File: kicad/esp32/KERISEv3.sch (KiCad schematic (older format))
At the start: 22 parts, among them P1 ANT, SW1 RESET, U1 ESP32, U2 XTAL, U3 FLASH

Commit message: 自動配線成功
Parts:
- removed C1, C6, C7: 0.1u, Capacitors_SMD:C_0201, symbol C_Small
- removed C12: 3.9p, Capacitors_SMD:C_0201, symbol C_Small
- removed C14: 2.4p, Capacitors_SMD:C_0201, symbol C_Small
- removed L1: 2.7n, Capacitors_SMD:C_0201, symbol L_Small
- removed P1: ANT, mouse:SMD_conn_2, symbol CONN_01X02
- C5: renamed from C8; value 3300p -> 3.3n
- U2: footprint Crystals:crystal_FA238-TSX3225 -> mouse:crystal_FA238-TSX3225
- U3: footprint Power_Integrations:SO-8 -> mouse:SOIJ-8_5.3x5.3mm_Pitch1.27mm
- renumbered C2 to C1, C3 to C2, C4 to C3, C5 to C4, C9 to C6, C10 to C7, C11 to C8, C13 to C9
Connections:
- wire segments 115 -> 106
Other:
- moved on the sheet: C4
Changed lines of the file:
@@
 $Descr A4 11693 8268
 encoding utf-8
-Sheet 1 13
+Sheet 1 14
 Title ""
 Date ""
@@
 Main
 $Comp
-L C_Small C1
-U 1 1 5894E609
-P 9500 1300
-F 0 "C1" H 9510 1370 50  0000 L CNN
-F 1 "0.1u" H 9510 1220 50  0000 L CNN
-F 2 "Capacitors_SMD:C_0201" H 9500 1300 50  0001 C CNN
-F 3 "" H 9500 1300 50  0000 C CNN
-	1    9500 1300
-	0    1    1    0
-$EndComp
-$Comp
-L C_Small C5
+L C_Small C4
 U 1 1 5894E774
-P 9500 2100
-F 0 "C5" H 9510 2170 50  0000 L CNN
-F 1 "0.1u" H 9510 2020 50  0000 L CNN
-F 2 "Capacitors_SMD:C_0201" H 9500 2100 50  0001 C CNN
-F 3 "" H 9500 2100 50  0000 C CNN
-	1    9500 2100
-	0    1    1    0
-$EndComp
-$Comp
-L C_Small C7
-U 1 1 5894E88A
-P 9500 2500
-F 0 "C7" H 9510 2570 50  0000 L CNN
-F 1 "0.1u" H 9510 2420 50  0000 L CNN
-F 2 "Capacitors_SMD:C_0201" H 9500 2500 50  0001 C CNN
-F 3 "" H 9500 2500 50  0000 C CNN
-	1    9500 2500
+P 9500 2300
+F 0 "C4" H 9510 2370 50  0000 L CNN
+F 1 "0.1u" H 9510 2220 50  0000 L CNN
+F 2 "Capacitors_SMD:C_0201" H 9500 2300 50  0001 C CNN
+F 3 "" H 9500 2300 50  0000 C CNN
+	1    9500 2300
 	0    1    1    0
 $EndComp
@@
 Text GLabel 5000 3600 0    50   Input ~ 0
 SPEAKER
-Text GLabel 5000 4400 0    50   Input ~ 0
+Text GLabel 5000 4000 0    50   Input ~ 0
 AXIS_~CS
-Text GLabel 5000 4000 0    50   Input ~ 0
+Text GLabel 5000 4100 0    50   Input ~ 0
 AXIS_SCK
 Text GLabel 5000 4200 0    50   Input ~ 0
 AXIS_MOSI
-Text GLabel 5000 4100 0    50   Input ~ 0
+Text GLabel 5000 4500 0    50   Input ~ 0
 AXIS_MISO
-Text GLabel 5000 4500 0    50   Input ~ 0
+Text GLabel 5000 4400 0    50   Input ~ 0
 BAT-VOL
 Text GLabel 5200 1500 0    50   Input ~ 0
@@
 $EndComp
 $Comp
-L C_Small C8
+L C_Small C5
 U 1 1 58A71512
 P 9700 4200
-F 0 "C8" H 9710 4270 50  0000 L CNN
-F 1 "3300p" H 9710 4120 50  0000 L CNN
+F 0 "C5" H 9710 4270 50  0000 L CNN
+F 1 "3.3n" H 9710 4120 50  0000 L CNN
 F 2 "Capacitors_SMD:C_0201" H 9700 4200 50  0001 C CNN
 F 3 "" H 9700 4200 50  0000 C CNN
@@
 $EndComp
 $Comp
-L C_Small C9
+L C_Small C6
 U 1 1 58A770D7
 P 10000 4200
-F 0 "C9" H 10010 4270 50  0000 L CNN
+F 0 "C6" H 10010 4270 50  0000 L CNN
 F 1 "0.01u" H 10010 4120 50  0000 L CNN
 F 2 "Capacitors_SMD:C_0201" H 10000 4200 50  0001 C CNN
@@
 $EndComp
 $Comp
-L C_Small C6
-U 1 1 58A93D5D
-P 9500 2300
-F 0 "C6" H 9510 2370 50  0000 L CNN
-F 1 "0.1u" H 9510 2220 50  0000 L CNN
-F 2 "Capacitors_SMD:C_0201" H 9500 2300 50  0001 C CNN
-F 3 "" H 9500 2300 50  0000 C CNN
-	1    9500 2300
-	0    1    1    0
-$EndComp
-$Comp
-L C_Small C3
+L C_Small C2
 U 1 1 58A9401A
 P 9500 1700
-F 0 "C3" H 9510 1770 50  0000 L CNN
+F 0 "C2" H 9510 1770 50  0000 L CNN
 F 1 "10u" H 9510 1620 50  0000 L CNN
 F 2 "Capacitors_SMD:C_0402" H 9500 1700 50  0001 C CNN
@@
 $EndComp
 $Comp
-L C_Small C2
+L C_Small C1
 U 1 1 58A94440
 P 9500 1500
-F 0 "C2" H 9510 1570 50  0000 L CNN
+F 0 "C1" H 9510 1570 50  0000 L CNN
 F 1 "0.1u" H 9510 1420 50  0000 L CNN
 F 2 "Capacitors_SMD:C_0201" H 9500 1500 50  0001 C CNN
@@
 F 0 "U3" H 5850 6450 60  0000 C CNN
 F 1 "FLASH" H 5900 6350 60  0000 C CNN
-F 2 "Power_Integrations:SO-8" H 5700 6250 60  0001 C CNN
+F 2 "mouse:SOIJ-8_5.3x5.3mm_Pitch1.27mm" H 5700 6250 60  0001 C CNN
 F 3 "" H 5700 6250 60  0000 C CNN
 	1    5700 6250
@@
 SDI/SD1
 $Comp
-L C_Small C13
+L C_Small C9
 U 1 1 58ABA852
 P 5100 5900
-F 0 "C13" H 5110 5970 50  0000 L CNN
+F 0 "C9" H 5110 5970 50  0000 L CNN
 F 1 "1u" H 5110 5820 50  0000 L CNN
 F 2 "Capacitors_SMD:C_0402" H 5100 5900 50  0001 C CNN
@@
 F 0 "U2" H 10300 5150 60  0000 C CNN
 F 1 "XTAL" H 10300 5000 60  0000 C CNN
-F 2 "Crystals:crystal_FA238-TSX3225" H 10300 4850 60  0001 C CNN
+F 2 "mouse:crystal_FA238-TSX3225" H 10300 4850 60  0001 C CNN
 F 3 "" H 10300 4850 60  0000 C CNN
 	1    10300 4850
@@
 	2600 5100 2500 5100
 Wire Wire Line
-	9200 1300 9400 1300
-Wire Wire Line
 	9200 1500 9400 1500
 Wire Wire Line
@@
 	9200 1900 9400 1900
 Connection ~ 9300 1700
-Wire Wire Line
-	9200 2100 9400 2100
 Connection ~ 9300 1900
-Wire Wire Line
-	9200 2300 9400 2300
 Connection ~ 9300 2100
 Wire Wire Line
-	9200 2500 9400 2500
-Connection ~ 9300 2300
-Connection ~ 9300 2500
-Wire Wire Line
-	9700 2100 9600 2100
-Wire Wire Line
 	9700 1900 9600 1900
-Connection ~ 9700 2100
-Wire Wire Line
-	9600 1300 9700 1300
 Connection ~ 9700 1900
 Connection ~ 9300 1300
@@
 	9700 3300 9600 3300
 Wire Wire Line
-	9700 2500 9600 2500
-Connection ~ 9700 2500
-Wire Wire Line
-	9700 2300 9600 2300
-Connection ~ 9700 2300
-Wire Wire Line
 	9600 1500 9700 1500
-Connection ~ 9700 1500
 Wire Wire Line
 	9700 1700 9600 1700
 Connection ~ 9700 1700
 Wire Wire Line
-	9700 1300 9700 2600
-Wire Wire Line
 	5100 6000 5100 6100
 Wire Wire Line
@@
 	9200 4000 10000 4000
 $Comp
-L C_Small C11
+L C_Small C8
 U 1 1 58ADFB26
 P 9700 5100
-F 0 "C11" H 9710 5170 50  0000 L CNN
+F 0 "C8" H 9710 5170 50  0000 L CNN
 F 1 "22p" H 9710 5020 50  0000 L CNN
 F 2 "Capacitors_SMD:C_0201" H 9700 5100 50  0001 C CNN
@@
 $EndComp
 $Comp
-L C_Small C10
+L C_Small C7
 U 1 1 58ADFC50
 P 9500 5100
-F 0 "C10" H 9510 5170 50  0000 L CNN
+F 0 "C7" H 9510 5170 50  0000 L CNN
 F 1 "22p" H 9510 5020 50  0000 L CNN
 F 2 "Capacitors_SMD:C_0201" H 9500 5100 50  0001 C CNN
@@
 $EndComp
 $Comp
-L C_Small C4
+L C_Small C3
 U 1 1 58AFD8EC
 P 9500 1900
-F 0 "C4" H 9510 1970 50  0000 L CNN
+F 0 "C3" H 9510 1970 50  0000 L CNN
 F 1 "10u" H 9510 1820 50  0000 L CNN
 F 2 "Capacitors_SMD:C_0402" H 9500 1900 50  0001 C CNN
@@
 	0    1    1    0
 $EndComp
-$Comp
-L L_Small L1
-U 1 1 58B5F4E4
-P 8000 5900
-F 0 "L1" H 8030 5940 50  0000 L CNN
-F 1 "2.7n" H 8030 5860 50  0000 L CNN
-F 2 "Capacitors_SMD:C_0201" H 8000 5900 50  0001 C CNN
-F 3 "" H 8000 5900 50  0000 C CNN
-	1    8000 5900
-	1    0    0    -1
-$EndComp
-$Comp
-L C_Small C12
-U 1 1 58B5F6D3
-P 7800 5700
-F 0 "C12" H 7810 5770 50  0000 L CNN
-F 1 "3.9p" H 7810 5620 50  0000 L CNN
-F 2 "Capacitors_SMD:C_0201" H 7800 5700 50  0001 C CNN
-F 3 "" H 7800 5700 50  0000 C CNN
-	1    7800 5700
-	0    1    1    0
-$EndComp
-$Comp
-L C_Small C14
-U 1 1 58B60E12
-P 7500 5900
-F 0 "C14" H 7510 5970 50  0000 L CNN
-F 1 "2.4p" H 7510 5820 50  0000 L CNN
-F 2 "Capacitors_SMD:C_0201" H 7500 5900 50  0001 C CNN
-F 3 "" H 7500 5900 50  0000 C CNN
-	1    7500 5900
-	1    0    0    -1
-$EndComp
-$Comp
-L GND #PWR013
-U 1 1 58B61357
-P 7500 6100
-F 0 "#PWR013" H 7500 5850 50  0001 C CNN
-F 1 "GND" H 7500 5950 50  0000 C CNN
-F 2 "" H 7500 6100 50  0000 C CNN
-F 3 "" H 7500 6100 50  0000 C CNN
-	1    7500 6100
-	1    0    0    -1
-$EndComp
-Wire Wire Line
-	7500 6100 7500 6000
-$Comp
-L GND #PWR014
-U 1 1 58B61565
-P 8000 6100
-F 0 "#PWR014" H 8000 5850 50  0001 C CNN
-F 1 "GND" H 8000 5950 50  0000 C CNN
-F 2 "" H 8000 6100 50  0000 C CNN
-F 3 "" H 8000 6100 50  0000 C CNN
-	1    8000 6100
-	1    0    0    -1
-$EndComp
-Wire Wire Line
-	8000 6100 8000 6000
-Wire Wire Line
-	8000 5800 8000 5700
-Wire Wire Line
-	7300 5700 7700 5700
-Wire Wire Line
-	7500 5700 7500 5800
-$Comp
-L CONN_01X02 P1
-U 1 1 58B61A43
-P 7100 5750
-F 0 "P1" H 7100 5900 50  0000 C CNN
-F 1 "ANT" V 7200 5750 50  0000 C CNN
-F 2 "mouse:SMD_conn_2" H 7100 5750 50  0001 C CNN
-F 3 "" H 7100 5750 50  0000 C CNN
-	1    7100 5750
-	-1   0    0    -1
-$EndComp
-$Comp
-L GND #PWR015
-U 1 1 58B61E88
-P 7300 6100
-F 0 "#PWR015" H 7300 5850 50  0001 C CNN
-F 1 "GND" H 7300 5950 50  0000 C CNN
-F 2 "" H 7300 6100 50  0000 C CNN
-F 3 "" H 7300 6100 50  0000 C CNN
-	1    7300 6100
-	1    0    0    -1
-$EndComp
-Wire Wire Line
-	7300 6100 7300 5800
-Connection ~ 7500 5700
-Connection ~ 8000 5700
-Text GLabel 8100 5700 2    50   Input ~ 0
+Text GLabel 2600 7300 2    50   Input ~ 0
 ANT
-Wire Wire Line
-	8100 5700 7900 5700
 Text GLabel 5200 1300 0    50   Input ~ 0
 ANT
@@
 Wire Wire Line
 	5000 2900 5200 2900
+Wire Wire Line
+	9300 2500 9200 2500
+Wire Wire Line
+	9200 2300 9400 2300
+Connection ~ 9300 2300
+Wire Wire Line
+	9300 1300 9200 1300
+Wire Wire Line
+	9700 1500 9700 2600
+Wire Wire Line
+	9300 2100 9200 2100
+Wire Wire Line
+	9600 2300 9700 2300
+Connection ~ 9700 2300
+$Sheet
+S 1500 7200 1000 200
+U 58A6C6D7
+F0 "Antena" 60
+F1 "Antena.sch" 60
+F2 "Antena_IN" I R 2500 7300 60
+$EndSheet
+Wire Wire Line
+	2600 7300 2500 7300
 $EndSCHEMATC

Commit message: 更新
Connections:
- net labels removed: LED_3, RESET
- wire segments 106 -> 104
- no-connect marks 2 -> 3

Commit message: ESP32の回路図を更新
BOOTに必要なピンを明記
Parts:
- U1: symbol ESP32 -> ESP32-RESCUE-KERISEv3
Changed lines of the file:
@@
 EESchema Schematic File Version 2
+LIBS:KERISEv3-rescue
 LIBS:power
 LIBS:device
@@
 NoConn ~ 5200 5100
 $Comp
-L ESP32 U1
+L ESP32-RESCUE-KERISEv3 U1
 U 1 1 58A3B0F8
 P 7200 3100

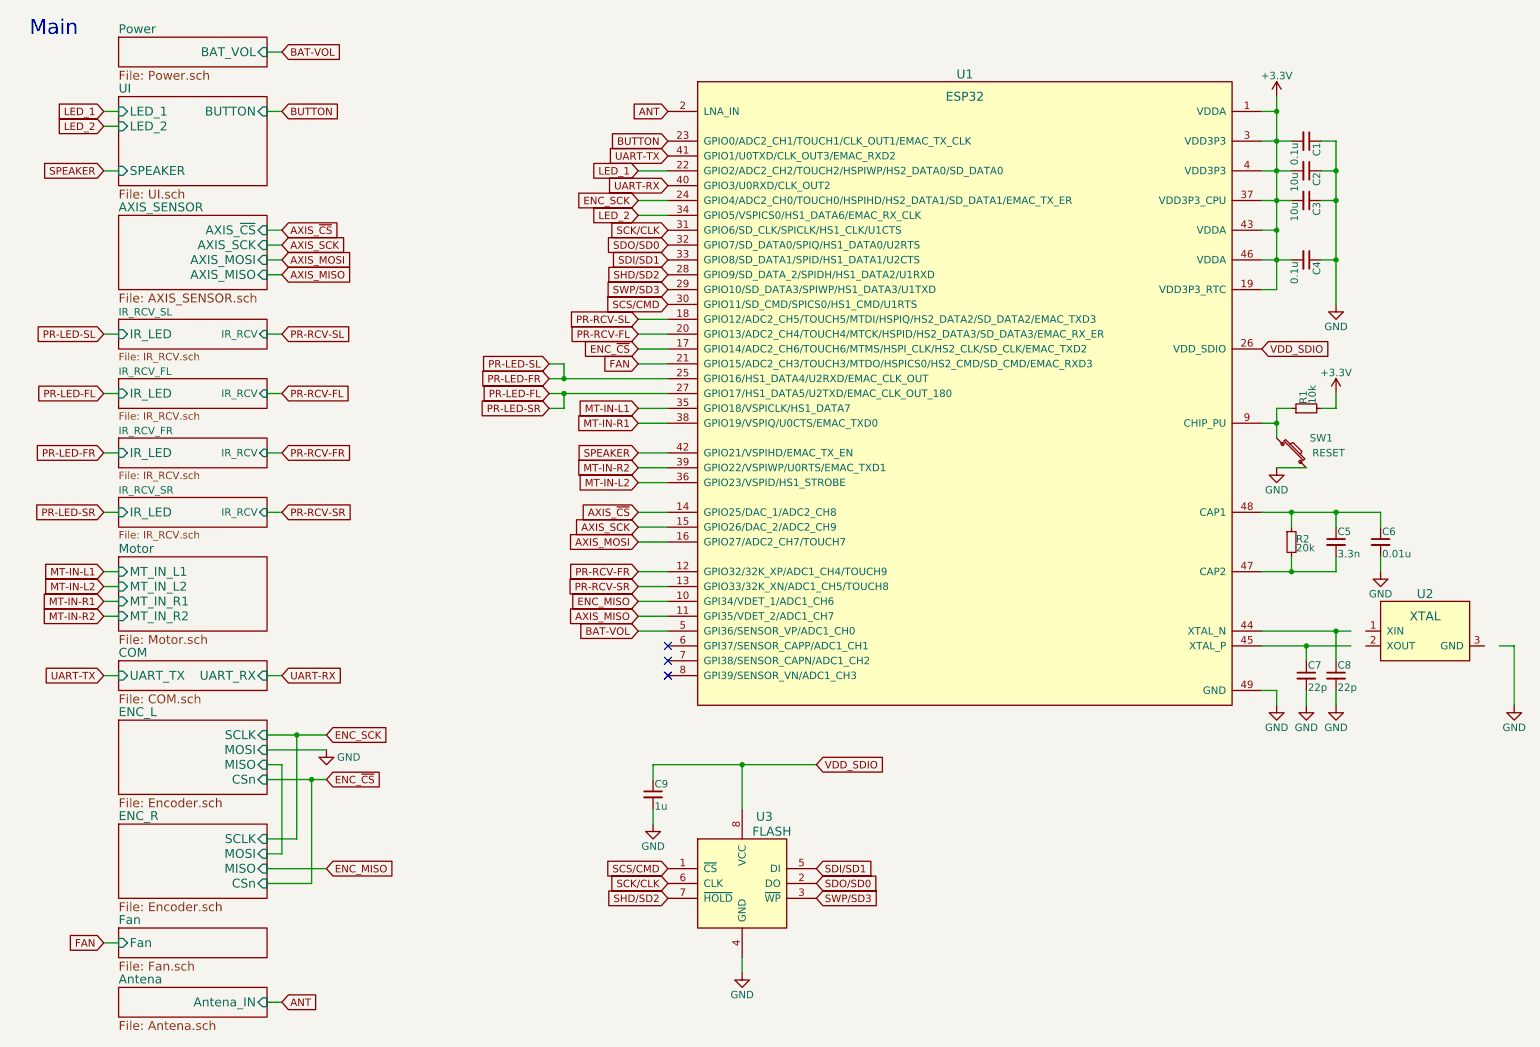
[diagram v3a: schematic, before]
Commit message: 2輪の基板を作成
部品を配置
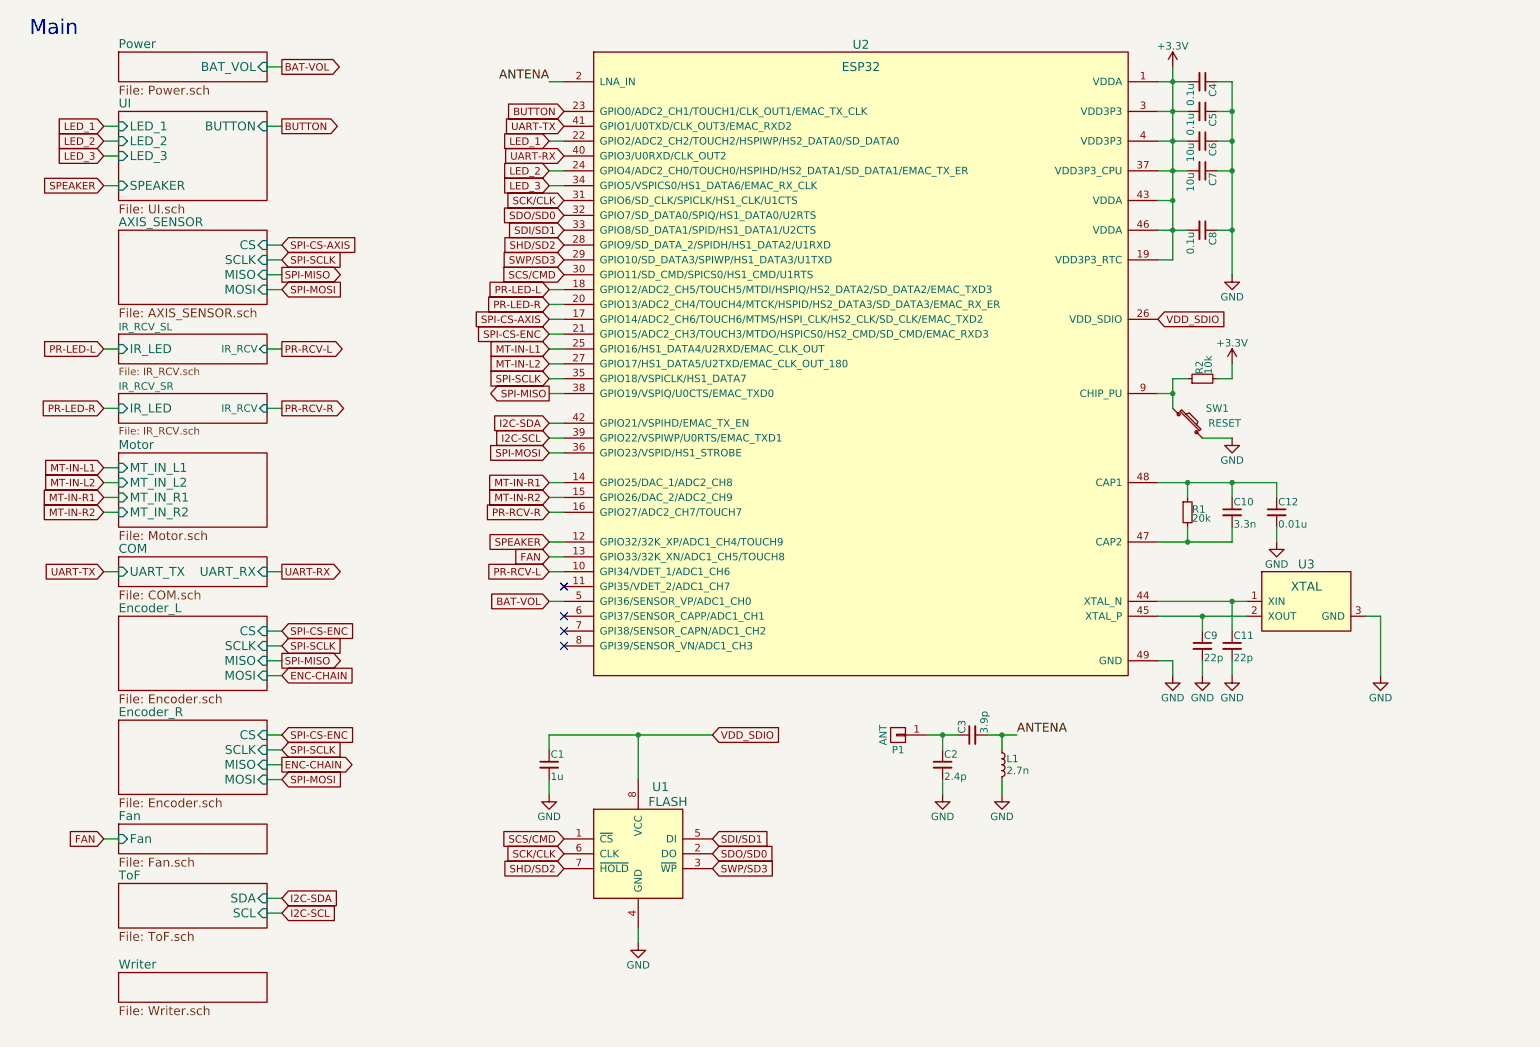
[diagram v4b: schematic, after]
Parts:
- added C2: 2.4p, Capacitors_SMD:C_0201, symbol C_Small
- added C3: 3.9p, Capacitors_SMD:C_0201, symbol C_Small
- added C4: 0.1u, Capacitors_SMD:C_0201, symbol C_Small
- added L1: 2.7n, Capacitors_SMD:C_0201, symbol L_Small
- added P1: ANT, mouse:SMD_conn_1, symbol CONN_01X01
- SW1: footprint Buttons_Switches_SMD:SW_SPST_KMR2 -> mouse:SW_PUSH
- U1: renamed from U3; footprint mouse:SOIJ-8_5.3x5.3mm_Pitch1.27mm -> mouse:DFN-8-1EP_6x5mm_Pitch1.27mm_SmallFlag
- renumbered C9 to C1, C5 to C10, C8 to C11, C6 to C12, C1 to C5, C2 to C6, C3 to C7, C4 to C8, C7 to C9, R2 to R1, R1 to R2, U1 to U2, U2 to U3
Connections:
- net AXIS_SCK is gone; now on net MT-IN-R2: U2.15 (GPIO26/DAC_2/ADC2_CH9)
- net AXIS_~CS is gone; now on net MT-IN-R1: U2.14 (GPIO25/DAC_1/ADC2_CH8)
- net ENC_SCK is gone; now on net LED_2: U2.24 (GPIO4/ADC2_CH0/TOUCH0/HSPIHD/HS2_DATA1/SD_DATA1/EMAC_TX_ER)
- net PR-LED-FL is gone; now on net MT-IN-L2: U2.27 (GPIO17/HS1_DATA5/U2TXD/EMAC_CLK_OUT_180)
- net PR-LED-FR is gone; now on net MT-IN-L1: U2.25 (GPIO16/HS1_DATA4/U2RXD/EMAC_CLK_OUT)
- net PR-RCV-FR is gone; now on net SPEAKER: U2.12 (GPIO32/32K_XP/ADC1_CH4/TOUCH9)
- net PR-RCV-SR is gone; now on net FAN: U2.13 (GPIO33/32K_XN/ADC1_CH5/TOUCH8)
- net +3V3: now also C4.2
- net FAN: no longer U2.21 (GPIO15/ADC2_CH3/TOUCH3/MTDO/HSPICS0/HS2_CMD/SD_CMD/EMAC_RXD3)
- net GND: now also U3.3 (GND), C2.2, C4.1, L1.2
- net LED_2: no longer U2.34 (GPIO5/VSPICS0/HS1_DATA6/EMAC_RX_CLK)
- net MT-IN-L1: no longer U2.35 (GPIO18/VSPICLK/HS1_DATA7)
- net MT-IN-L2: no longer U2.36 (GPIO23/VSPID/HS1_STROBE)
- net MT-IN-R1: no longer U2.38 (GPIO19/VSPIQ/U0CTS/EMAC_TXD0)
- net MT-IN-R2: no longer U2.39 (GPIO22/VSPIWP/U0RTS/EMAC_TXD1)
- net SPEAKER: no longer U2.42 (GPIO21/VSPIHD/EMAC_TX_EN)
- net at C11.1, U2.44 (XTAL_N): now also U3.1 (XIN)
- net at C9.1, U2.45 (XTAL_P): now also U3.2 (XOUT)
- net ANT renamed ANTENA
- net ANTENA: now also C3.2, L1.1
- net AXIS_MISO: no longer names the net of U2.11 (GPI35/VDET_2/ADC1_CH7)
- net AXIS_MOSI renamed PR-RCV-R
- net ENC_MISO renamed PR-RCV-L
- net ENC_~CS renamed SPI-CS-AXIS
- net PR-RCV-FL renamed PR-LED-R
- net PR-RCV-SL renamed PR-LED-L
- new net: C2.1, C3.1, P1.1 (P1)
- new net I2C-SCL: U2.39 (GPIO22/VSPIWP/U0RTS/EMAC_TXD1)
- new net I2C-SDA: U2.42 (GPIO21/VSPIHD/EMAC_TX_EN)
- new net LED_3: U2.34 (GPIO5/VSPICS0/HS1_DATA6/EMAC_RX_CLK)
- new net SPI-CS-ENC: U2.21 (GPIO15/ADC2_CH3/TOUCH3/MTDO/HSPICS0/HS2_CMD/SD_CMD/EMAC_RXD3)
- new net SPI-MISO: U2.38 (GPIO19/VSPIQ/U0CTS/EMAC_TXD0)
- new net SPI-MOSI: U2.36 (GPIO23/VSPID/HS1_STROBE)
- new net SPI-SCLK: U2.35 (GPIO18/VSPICLK/HS1_DATA7)
- no-connect marks 3 -> 4
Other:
- moved on the sheet: C1, C10, C11, C12, C5, C6, C7, C8, C9, R1, R2, SW1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
